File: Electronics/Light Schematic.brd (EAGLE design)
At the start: 160 x 100 mm, 9 parts, among them IC1 7805T, U1 328P

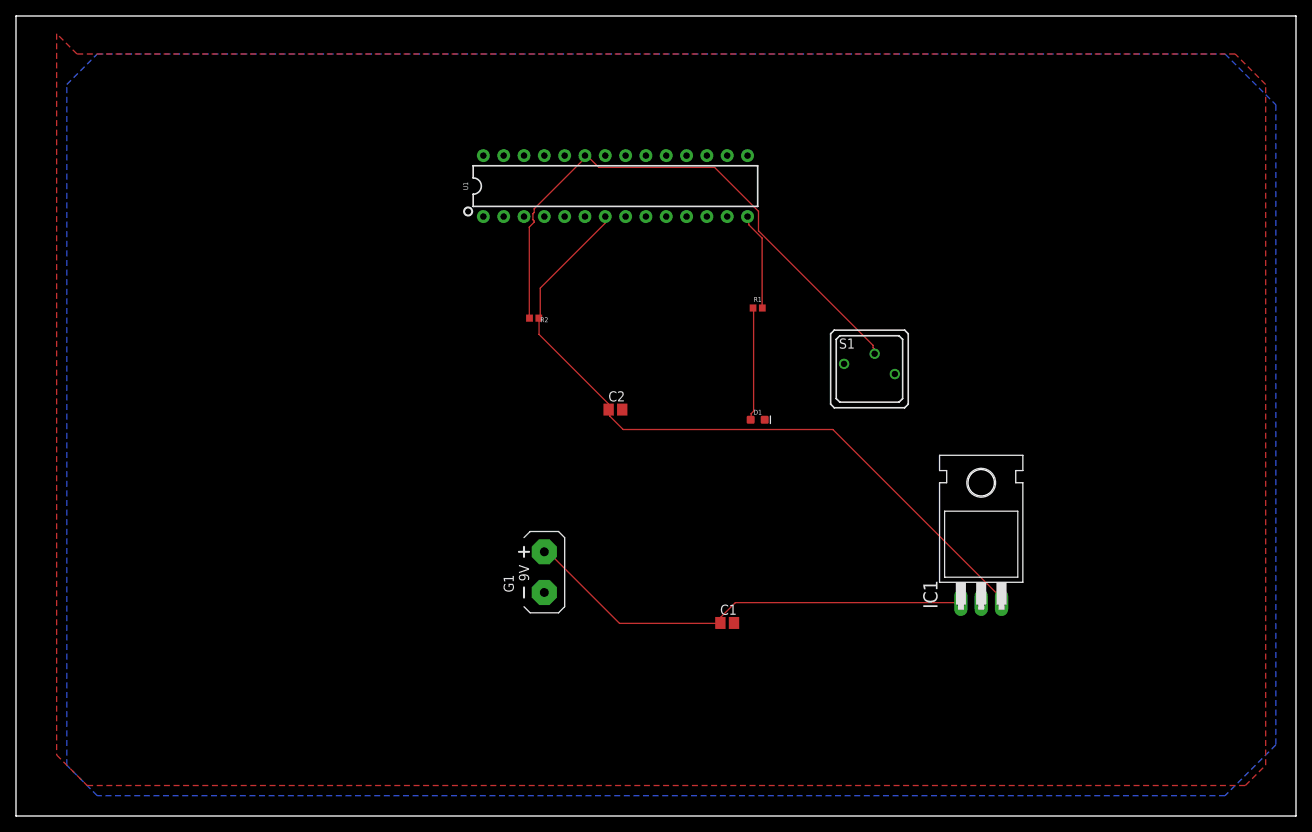
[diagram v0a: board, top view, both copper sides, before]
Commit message: updated PCB and schematic w crystal oscillator
and 2 capacitors
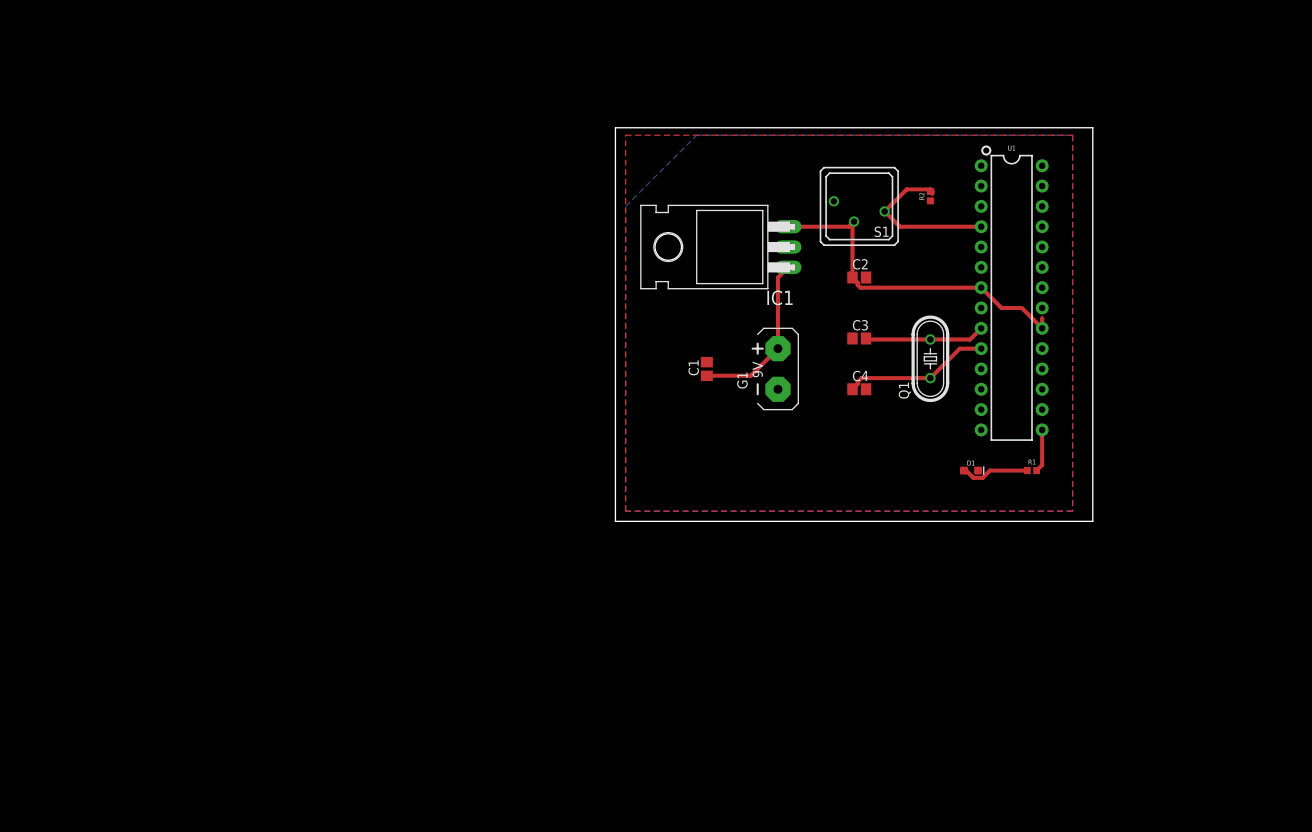
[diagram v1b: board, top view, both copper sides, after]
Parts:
- added C3, C4: 22pF, adafruit:C0805
- added Q1: (no value), adafruit:HC49/S
- C2: value 50µF -> 30µF
- R1: value 100K -> 100
- moved R2 51.8 mm to (114.3, 77.5), turned to 90 degrees
- moved U1 51.5 mm to (124.5, 64.8), turned to 270 degrees
- moved IC1 48.5 mm to (86.4, 71.1), turned to 90 degrees
- moved R1 39.9 mm to (127.0, 43.2)
- moved G1 38.7 mm to (95.2, 55.9)
- moved C2 34.7 mm to (105.4, 67.3)
- moved C1 31.9 mm to (86.4, 55.9), turned to 90 degrees
- moved D1 27.4 mm to (119.4, 43.2)
- moved S1 20.4 mm to (105.4, 76.2), turned to 180 degrees
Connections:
- new net N$3: C3.2, Q1.2, U1.9
- new net N$6: R1.2, U1.15
- new net N$7: C4.1, Q1.1, U1.10
- net 5V: now also S1.B, U1.20; no longer R2.2
- net GND: now also C3.1, C4.2, R2.1; no longer S1.A1
- net N$2: now also R2.2, S1.A1, U1.4; no longer R2.1, S1.B, U1.23
- net N$4: no longer R1.2
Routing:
- net N$2: track 71.7 -> 20.7 mm
- net 5V: track 91.1 -> 43.3 mm
- net N$1: track 57.2 -> 21.0 mm
- net N$7: track 0.00 -> 18.4 mm
- net N$3: track 0.00 -> 15.0 mm
- net N$4: track 12.2 -> 0.00 mm
- net N$5: track 14.2 -> 8.67 mm
- net N$6: track 0.00 -> 5.37 mm
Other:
- board size 160 x 100 mm -> 59.7 x 49.2 mm

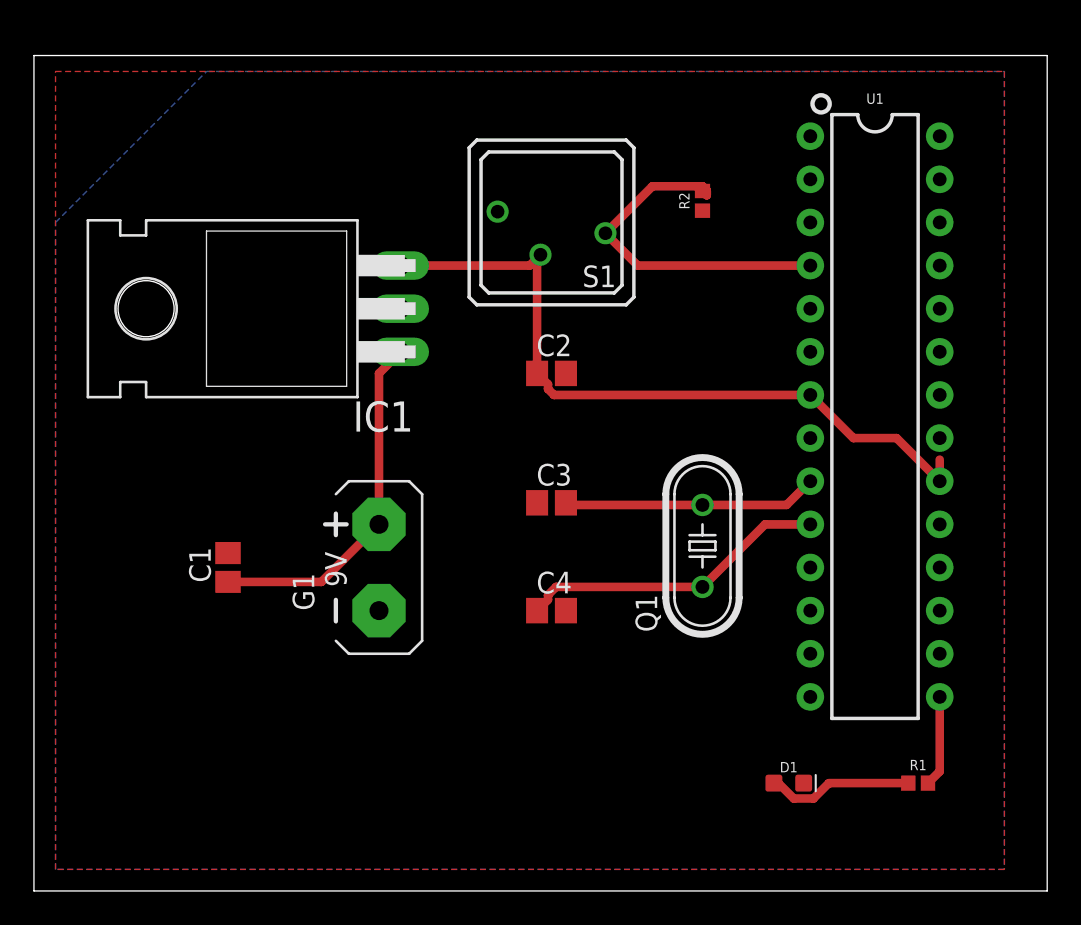
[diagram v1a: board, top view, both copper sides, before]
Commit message: updated light box schematic and PCB
- connected pin 8 and pin 22
- changed the battery to header pins
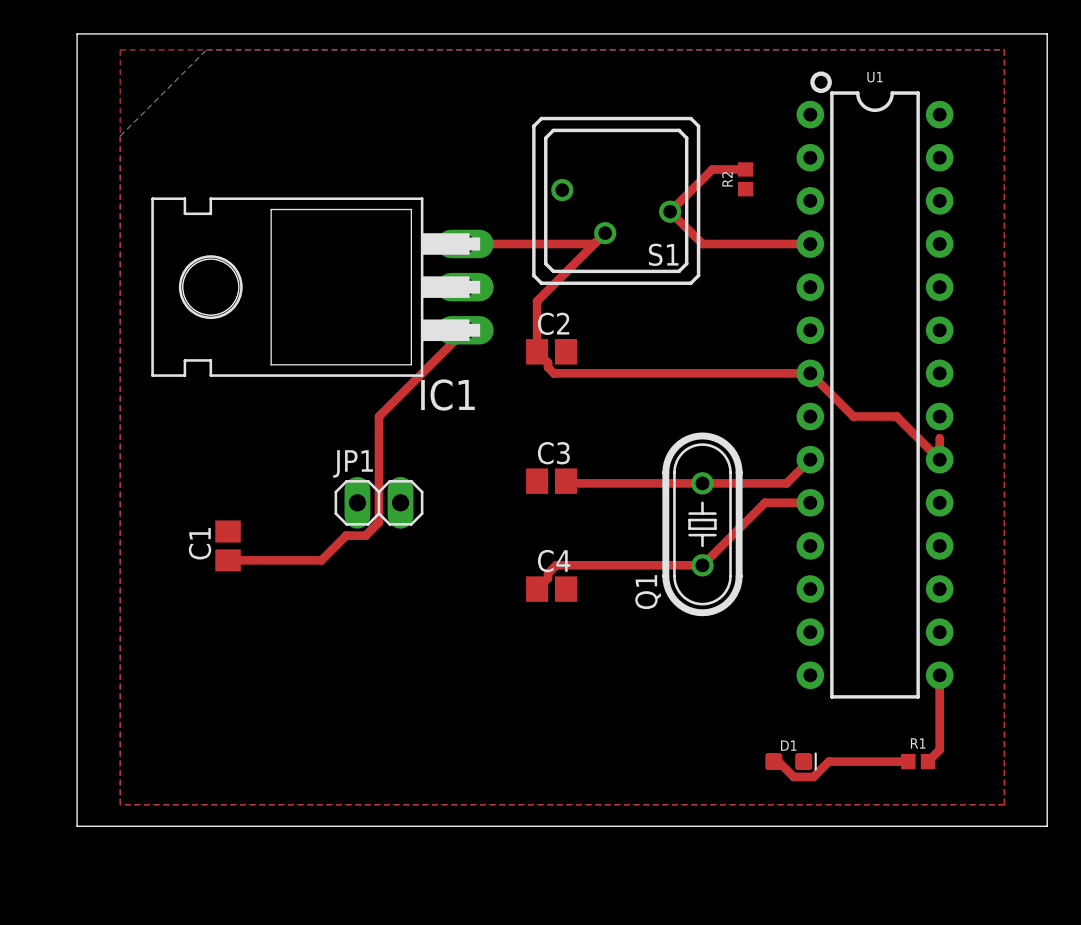
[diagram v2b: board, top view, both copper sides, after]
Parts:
- removed G1: AB9V, battery:AB9V
- added JP1: (no value), pinhead:1X02
- moved IC1 4.02 mm to (90.2, 72.4)
- moved S1 4.02 mm to (109.2, 77.5)
- moved R2 2.84 mm to (116.8, 78.7)
- moved U1 1.27 mm to (124.5, 66.0)
- moved C3 1.27 mm to (105.4, 61.0)
- moved D1 1.27 mm to (119.4, 44.5)
- moved Q1 1.27 mm to (114.3, 58.4)
- moved R1 1.27 mm to (127.0, 44.5)
- moved C1 1.27 mm to (86.4, 57.1)
- moved C2 1.27 mm to (105.4, 68.6)
- moved C4 1.27 mm to (105.4, 54.6)
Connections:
- net GND: now also U1.22; no longer G1.-
- net N$1: no longer G1.+
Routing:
- net N$2: track 20.7 -> 14.5 mm
- net N$1: track 21.0 -> 23.2 mm
- net 5V: track 43.3 -> 44.9 mm
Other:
- board size 59.7 x 49.2 mm -> 57.1 x 46.7 mm

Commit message: updated light box board
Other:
- board size 57.1 x 46.7 mm -> 58.4 x 46.7 mm
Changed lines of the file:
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@@
 <drawing>
 <settings>
-<setting alwaysvectorfont="no"/>
+<setting alwaysvectorfont="yes"/>
 <setting verticaltext="up"/>
 </settings>
@@
 <layer number="43" name="vRestrict" color="2" fill="10" visible="yes" active="yes"/>
 <layer number="44" name="Drills" color="7" fill="1" visible="no" active="yes"/>
-<layer number="45" name="Holes" color="7" fill="1" visible="no" active="yes"/>
+<layer number="45" name="Holes" color="7" fill="1" visible="yes" active="yes"/>
 <layer number="46" name="Milling" color="3" fill="1" visible="no" active="yes"/>
 <layer number="47" name="Measures" color="7" fill="1" visible="no" active="yes"/>
@@
 </layers>
 <board>
+<fusionsync huburn="a.cGVyc29uYWw6dWUyYTUyZjgw" projecturn="a.cGVyc29uYWw6dWUyYTUyZjgwIzIwMTgwMTE4MTEyOTk4MTUx" f3durn="urn:adsk.wipprod:dm.lineage:dA__Lqd2TvqUaQ0AZ8b9gA" pcbguid="82a3f82d-7d55-47ad-b88b-db349eaa616a" lastpulledtime="" lastsyncedchangeguid="e95ea2e0-2476-fb2a-1e0b-62e5c6800621"/>
 <plain>
-<wire x1="77.47" y1="40.64" x2="134.6" y2="40.64" width="0" layer="20"/>
-<wire x1="134.6" y1="40.64" x2="134.6" y2="87.3" width="0" layer="20"/>
-<wire x1="134.6" y1="87.3" x2="77.47" y2="87.3" width="0" layer="20"/>
+<wire x1="77.47" y1="40.64" x2="135.87" y2="40.64" width="0" layer="20"/>
+<wire x1="135.87" y1="40.64" x2="135.87" y2="87.3" width="0" layer="20"/>
+<wire x1="135.87" y1="87.3" x2="77.47" y2="87.3" width="0" layer="20"/>
 <wire x1="77.47" y1="87.3" x2="77.47" y2="40.64" width="0" layer="20"/>
+<hole x="82.55" y="83.82" drill="3.175"/>
+<hole x="82.55" y="44.45" drill="3.175"/>
+<hole x="132.08" y="44.45" drill="3.175"/>
+<hole x="132.08" y="83.82" drill="3.175"/>
 </plain>
 <attributes>
@@
 <vertex x="80.01" y="41.91"/>
 <vertex x="80.01" y="86.36"/>
-<vertex x="132.08" y="86.36"/>
-<vertex x="132.08" y="41.91"/>
+<vertex x="134.62" y="86.36"/>
+<vertex x="134.62" y="41.91"/>
 </polygon>
 <polygon width="0.1524" layer="16">
-<vertex x="80.01" y="81.28"/>
-<vertex x="85.09" y="86.36"/>
-<vertex x="132.08" y="86.36"/>
-<vertex x="132.08" y="41.91"/>
+<vertex x="80.01" y="82.55"/>
+<vertex x="83.82" y="86.36"/>
+<vertex x="134.62" y="86.36"/>
+<vertex x="134.62" y="41.91"/>
 <vertex x="80.01" y="41.91"/>
 </polygon>
@@
 </note>
 <note version="8.3" severity="warning">
+Since Version 8.3, EAGLE supports Fusion synchronisation.
+This feature will not be available in this version and saving
+the document will break the link to the Fusion PCB feature.
+</note>
+<note version="8.3" severity="warning">
